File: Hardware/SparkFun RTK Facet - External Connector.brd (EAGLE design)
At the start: 54 x 20 mm, 40 parts, among them J1 FPC_12_0.5MM2, J4 Qwiic, J5 u-blox USB, J6 FPC_12_0.5MM2

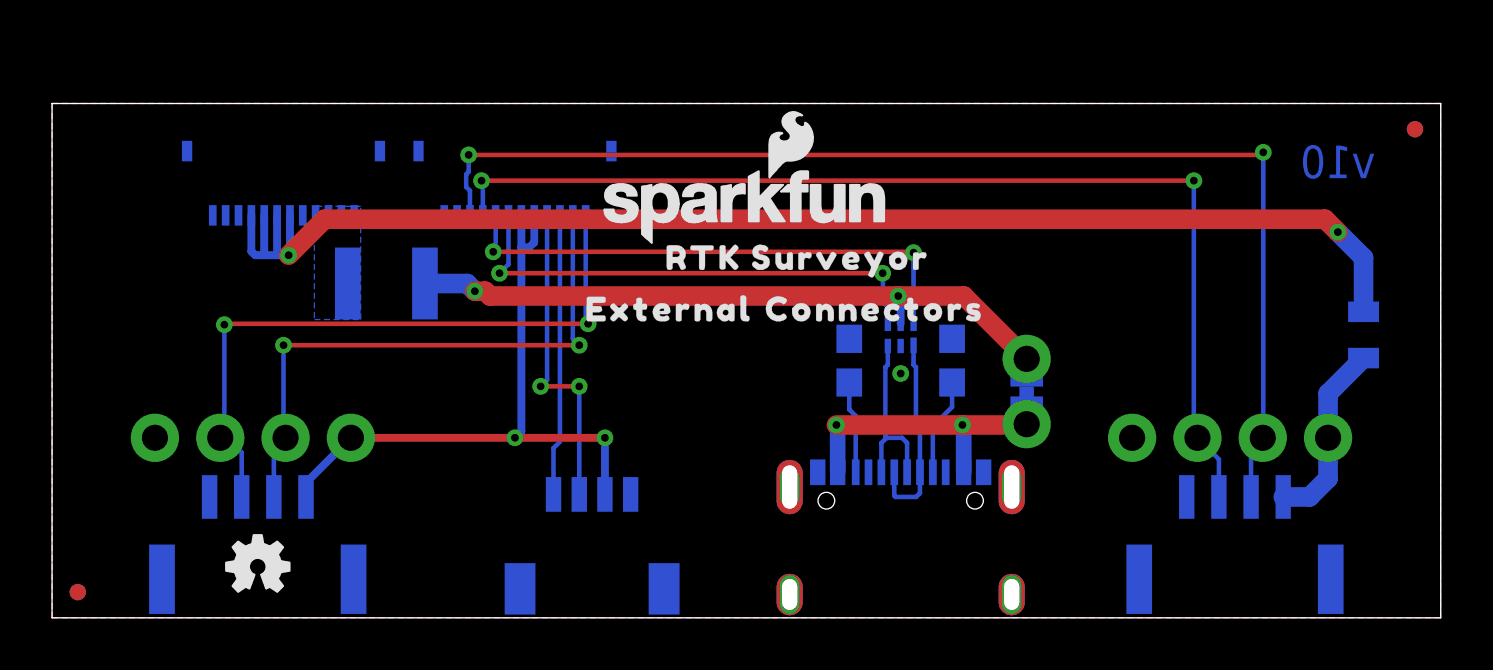
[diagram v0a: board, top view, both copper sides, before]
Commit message: Move display connector to side so overlay connector can be center. Notch PCBs. Add dummy PCB height. Add dummy retention plate.
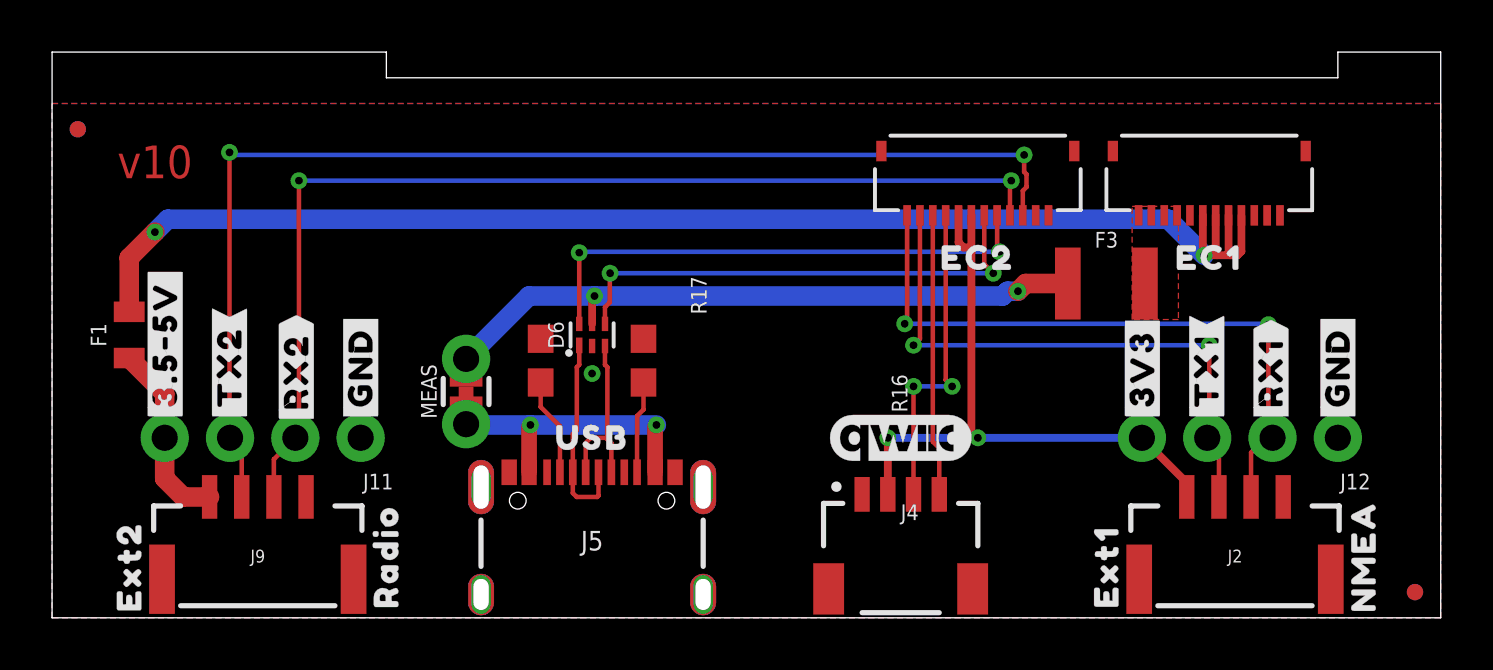
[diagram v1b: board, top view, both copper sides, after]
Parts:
- moved JP21 52.0 mm to (53.0, 1.00), flipped to the top
- moved JP61 52.0 mm to (1.00, 19.0), flipped to the top
- moved JP71 52.0 mm to (53.0, 1.00), flipped to the bottom
- moved JP81 52.0 mm to (1.00, 19.0), flipped to the bottom
- moved F1 48.0 mm to (3.00, 11.0), flipped to the top
- moved U$6 48.0 mm to (3.00, 2.00), flipped to the top
- moved U$7 48.0 mm to (51.0, 2.40), flipped to the top
- moved J12 46.0 mm to (50.0, 7.00), flipped to the top
- moved U$82 46.0 mm to (50.0, 7.50), flipped to the top
- moved U$23 45.2 mm to (4.40, 7.50), flipped to the top
- moved U$68 40.8 mm to (47.4, 7.50), flipped to the top
- moved U$40 40.2 mm to (6.90, 7.50), flipped to the top
- moved J2 38.0 mm to (46.0, 1.40), flipped to the top
- moved J9 38.0 mm to (8.00, 1.40), flipped to the top
- moved LOGO1 38.0 mm to (46.0, 2.00), flipped to the bottom
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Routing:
- added copper zone on layer 1, net V_USB
- removed copper zone on layer 16, net V_USB
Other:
- board size 54 x 20 mm -> 54 x 22 mm

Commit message: Update PROD ID on 12 pin connector. Add gerbers for v10.
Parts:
- J1, J6: value FPC_12_0.5MM2 -> FPC_12_0.5MM_BACKFLIP; device RTK Facet:FPC_12_FLIP_DOUBLESIDED_2 -> RTK Facet:FPC_12_DOUBLESIDED_BACKFLIP
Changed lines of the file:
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@@
 <setting verticaltext="up"/>
 </settings>
-<grid distance="1" unitdist="mm" unit="mm" style="lines" multiple="1" display="yes" altdistance="0.1" altunitdist="mm" altunit="mm"/>
+<grid distance="0.05" unitdist="inch" unit="inch" style="lines" multiple="1" display="yes" altdistance="0.005" altunitdist="inch" altunit="inch"/>
 <layers>
 <layer number="1" name="Top" color="4" fill="1" visible="yes" active="yes"/>
@@
 <attribute name="VALUE" x="41" y="11.603" size="0.6096" layer="27" font="vector" ratio="20" align="top-center"/>
 </element>
-<element name="J1" library="RTK Facet" package="FPC_12_FLIP_DOUBLESIDED_2" value="FPC_12_0.5MM2" x="45" y="17" smashed="yes" rot="R180"/>
-<element name="J6" library="RTK Facet" package="FPC_12_FLIP_DOUBLESIDED_2" value="FPC_12_0.5MM2" x="36" y="17" smashed="yes" rot="R180"/>
+<element name="J1" library="RTK Facet" package="FPC_12_DOUBLESIDED_BACKFLIP" value="FPC_12_0.5MM_BACKFLIP" x="45" y="17" smashed="yes" rot="R180">
+<attribute name="PROD_ID" value="CONN-15766" x="45" y="17" size="1.778" layer="27" rot="R180" display="off"/>
+</element>
+<element name="J6" library="RTK Facet" package="FPC_12_DOUBLESIDED_BACKFLIP" value="FPC_12_0.5MM_BACKFLIP" x="36" y="17" smashed="yes" rot="R180">
+<attribute name="PROD_ID" value="CONN-15766" x="36" y="17" size="1.778" layer="27" rot="R180" display="off"/>
+</element>
 </elements>
 <signals>
@@
 <contactref element="J6" pad="2"/>
 <via x="21" y="9.5" extent="1-16" drill="0.3"/>
+<wire x1="47.25" y1="15.65" x2="47.75" y2="15.65" width="0" layer="19" extent="1-1"/>
+<wire x1="46.75" y1="15.65" x2="47.25" y2="15.65" width="0" layer="19" extent="1-1"/>
+<wire x1="38.75" y1="15.65" x2="46.75" y2="15.65" width="0" layer="19" extent="1-1"/>
+<wire x1="38.25" y1="15.65" x2="38.75" y2="15.65" width="0" layer="19" extent="1-1"/>
+<wire x1="50" y1="7" x2="47.75" y2="15.65" width="0" layer="19" extent="1-1"/>
+<wire x1="47.875" y1="4.7" x2="50" y2="7" width="0" layer="19" extent="1-1"/>
+<wire x1="31.5" y1="4.8" x2="38.25" y2="15.65" width="0" layer="19" extent="1-1"/>
+<wire x1="25.318" y1="5.085" x2="31.5" y2="4.8" width="0" layer="19" extent="1-1"/>
+<wire x1="24.225" y1="5.66" x2="25.318" y2="5.085" width="0" layer="19" extent="1-1"/>
+<wire x1="25.318" y1="0.905" x2="25.318" y2="5.085" width="0" layer="19" extent="1-1"/>
+<wire x1="21" y1="9.5" x2="24.225" y2="5.66" width="0" layer="19" extent="1-1"/>
+<wire x1="21" y1="10.57" x2="21" y2="9.5" width="0" layer="19" extent="1-1"/>
+<wire x1="23" y1="10.85" x2="21" y2="10.57" width="0" layer="19" extent="1-1"/>
+<wire x1="19" y1="10.85" x2="21" y2="10.57" width="0" layer="19" extent="1-1"/>
+<wire x1="17.775" y1="5.66" x2="21" y2="9.5" width="0" layer="19" extent="1-1"/>
+<wire x1="16.682" y1="5.085" x2="17.775" y2="5.66" width="0" layer="19" extent="1-1"/>
+<wire x1="16.682" y1="0.905" x2="16.682" y2="5.085" width="0" layer="19" extent="1-1"/>
+<wire x1="12" y1="7" x2="16.682" y2="5.085" width="0" layer="19" extent="1-1"/>
+<wire x1="9.875" y1="4.7" x2="12" y2="7" width="0" layer="19" extent="1-1"/>
 </signal>
 <signal name="ESP_22/SCL">
@@
 <vertex x="42" y="11.6"/>
 </polygon>
+<wire x1="43.25" y1="15.65" x2="43.75" y2="15.65" width="0" layer="19" extent="1-1"/>
+<wire x1="42.75" y1="15.65" x2="43.25" y2="15.65" width="0" layer="19" extent="1-1"/>
+<wire x1="42.25" y1="15.65" x2="42.75" y2="15.65" width="0" layer="19" extent="1-1"/>
+<wire x1="42.5" y1="13" x2="42.75" y2="15.65" width="0" layer="19" extent="1-1"/>
 </signal>
 <signal name="VIN1" class="1">
